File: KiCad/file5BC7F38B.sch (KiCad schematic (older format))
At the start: 74 parts, among them J301 DB9_Female, J302 Conn_01x06, J303 DB9_Male, P301 ISP/PDI, P302 Thru, P304 Header, Q301 PN2222A, SW301 SPST, U301 DS3231, U302 ATmega1284P-AU, U303 LP2992, U304 SI5351A, U305 74HC1G08, U306 LP2992, U307 SN74CB3Q3305, U308 LP2992, X301 ASTX-H11-25.MHZ, Y301 20 MHz

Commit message: AVR128DA48 Redesign
Kicad updates for new FlexFox design
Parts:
- removed TP301: I2C1, Pin_Headers:Pin_Header_Straight_1x03, symbol Connector_Generic:Conn_01x03
- removed U302: ATmega1284P-AU, Housings_QFP:TQFP-44_10x10mm_Pitch0.8mm, symbol MCU_Microchip_ATmega:ATmega1284P-AU
- removed U306: LP2992, TO_SOT_Packages_SMD:SOT-23-5, symbol Regulator_Linear:LP2992
- removed U307: SN74CB3Q3305, Housings_SSOP:TSSOP-8_3x3mm_Pitch0.65mm, symbol Interface:SN74CB3Q3305
- removed W301: TEST_1P, Measurement_Points:Measurement_Point_Square-SMD-Pad_Small, symbol FlexFox80-rescue:TEST_1P-ARDF-2-Band-MiniTx-rescue
- removed Y301: 20 MHz, Crystals:CSTNE20M0V53Z000R0, symbol Device:Resonator_Small
- added J304: Conn_01x10, symbol Connector_Generic:Conn_01x10
- added R314: 560k, Resistors_SMD:R_0805, symbol Device:R
- added R315, R316: 10k, Resistors_SMD:R_0805, symbol Device:R
- added TP301: I2C1, Pin_Headers:Pin_Header_Straight_1x04, symbol Connector_Generic:Conn_01x04
- added U302: AVR128DA48, TQFP48_PT_MCH, symbol FlexFox80-rescue:AVR128DA48-I_PT-MCU_Microchip_AVR
- added U306: LT1763CS8-5, Housings_SOIC:SOIC-8_3.9x4.9mm_Pitch1.27mm, symbol Regulator_Linear:LT1763CS8-5
- C301: LCSC Part Number (none) -> C344171
- C302, C306, C307, C308, C309, C311, C316, C319, C320: LCSC Part Number (none) -> C360619
- C303, C313, C314, C315, C317, C318: LCSC Part Number (none) -> C162420
- C304, C305: LCSC Part Number (none) -> C84416
- C310, C312: LCSC Part Number (none) -> C342818
- D301: LCSC Part Number (none) -> C152486
- D304: LCSC Part Number (none) -> C98224
- D305: LCSC Part Number (none) -> C72037
- D306, D307: LCSC Part Number (none) -> C2655331
- Q301: LCSC Part Number (none) -> C194252
- R301, R302: LCSC Part Number (none) -> C114564
- R303, R305, R306, R307, R310, R311: LCSC Part Number (none) -> C38522
- R304: LCSC Part Number (none) -> C96347
- R308, R313: LCSC Part Number (none) -> C103905
- R309: LCSC Part Number (none) -> C114561
- R312: LCSC Part Number (none) -> C352198
- RV301: LCSC Part Number (none) -> C719176
- SW301: LCSC Part Number (none) -> C221877
- U301: LCSC Part Number (none) -> C2651514
- U303, U308: value LP2992 -> LD2985BM33R; Description IC REG LINEAR 3.3V 250MA SOT23-5 -> IC REG LINEAR 3.3V 150MA SOT23-5; Digi-Key Part No. LP2992AIM5-3.3/NOPBCT-ND -> 497-3499-1-ND; LCSC Part Number (none) -> C222396; Link <a href=\"https://www.digikey.com/products/en?keywords=LP29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 -> <a href=\"https://www.digikey.com/products/en?keywords=497-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; Manufacturer Texas Instruments -> STMicroelectronics; Manufacturer PN LP2992AIM5-3.3/NOPB -> LD2985BM33R
- U304: LCSC Part Number (none) -> C529366
- U305: LCSC Part Number (none) -> C108694
- X301: value ASTX-H11-25.MHZ -> 25.MHZ TCXO; Description XTAL OSC TCXO 25.0000MHZ HCMOS -> XTAL OSC TCXO 25MHZ CLPSNW; Digi-Key Part No. 535-12039-1-ND -> 2780-I537-2O7-25.000MHZCT-ND; Link <a href=\"https://www.digikey.com/products/en?keywords=535-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 -> <a href=\"https://www.digikey.com/products/en?keywords=2780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; Manufacturer PN ASTX-H11-25.000MHZ-T -> I537-2O7-25.000 MHZ
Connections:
- net labels added: 32KHZ_SQUAREWAVE, ADC0, ADC1, ADC2, DAC0, DAC_OUTPUT, FET_DRIVER_ENABLE, PA3, PA4, PA5, PA6, PA7, PB5, PE2, PE3, PF2, PF3, PF4, PF5, PF6, RXD4, SCL0, SCL1, SDA0, SDA1, TXD4, WIFI_RX, WIFI_TX
- net labels removed: ADC6, DI_SCL, DI_SDA, DI_TXD0, HF_ENABLE, INT2, MISO, MOSI, PB3, PC2, PC3, PD4, PD5, PD6, PD7, RXD0, SCK, SCL, SDA, TXD0
- wire segments 314 -> 334
- no-connect marks 22 -> 24
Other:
- note added: "FTDI SERIAL ADAPTER"
- note added: "Future Display Interface"
- note removed: "FTDI PROGRAMMING ADAPTER"
- moved on the sheet: D304, D305, J302, J303, P301, R301, R302, R304, SW301, TP302

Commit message: Updates for AVR128DA48
o Board changes
o Gerbers updated
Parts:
- removed C304: 10uF, Capacitors_SMD:C_0805, symbol Device:C_Small
- removed C309, C316: 100nF, Capacitors_SMD:C_0805, symbol Device:C_Small
- removed unit 2 of D301
- removed R305: 10k, Resistors_SMD:R_0805, symbol Device:R
- added J305, J306, J307: Conn_01x02, Pin_Headers:Pin_Header_Straight_1x02, symbol Connector_Generic:Conn_01x02
- J304: footprint (none) -> Pin_Headers:Pin_Header_Straight_1x10; Digi-Key Part No. (none) -> np; Link (none) -> np; Manufacturer (none) -> np
- U302: footprint TQFP48_PT_MCH -> Housings_QFP:TQFP-48_7x7mm_Pitch0.5mm
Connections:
- net GND: now also J305.1 (Pin_1), J306.1 (Pin_1), J307.1 (Pin_1)
- net PC7: now also J305.2 (Pin_2)
- net at D305.2 (A), R302.1: now also J306.2 (Pin_2)
- net at D304.2 (A), R301.1: now also J307.2 (Pin_2)
- net ~RESET~ renamed PF6
- no-connect marks 24 -> 26
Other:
- moved on the sheet: D304, D305, R301, R302, SW301, TP302

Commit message: Updates
o Added fan control
o Fixed pinout for load switch device
o Updated gerbers
o Updated BOM
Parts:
- added C304: 10uF, Capacitors_SMD:C_0805, symbol Device:C_Small
- added J308: Conn_01x02, Pin_Headers:Pin_Header_Straight_1x02, symbol Connector_Generic:Conn_01x02
- added U307: TPS22810DBVT, TO_SOT_Packages_SMD:SOT-23-6, symbol Power_Management:TPS22810DBVT
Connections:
- net GND: now also C304.2, U307.2 (GND)
- net PA1 renamed FAN_ENABLE
- net FAN_ENABLE: now also U307.3 (EN/UVLO)
- new net: J308.2 (Pin_2), U307.1 (VIN)
- new net: C304.1, J308.1 (Pin_1), U307.6 (VOUT)
- no-connect marks 26 -> 27
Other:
- note added: "OPTIONAL FAN CONTROL"
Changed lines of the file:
@@
 Connection ~ 8150 7050
 NoConn ~ 7800 4150
-NoConn ~ 7800 4050
 Text Notes 1400 4800 1    39   ~ 8
 I2C pull-ups can be provided by uC \nport pin pull-ups on SCL and SDA.
@@
 Wire Wire Line
 	10950 5600 10950 5300
-Wire Bus Line
-	7700 3300 7700 8000
 Connection ~ 10950 5300
 Wire Wire Line
@@
 	0    1    1    0
 $EndComp
+$Comp
+L Power_Management:TPS22810DBVT U307
+U 1 1 6203E823
+P 15100 3900
+F 0 "U307" H 15100 4267 50  0000 C CNN
+F 1 "TPS22810DBVT" H 15100 4176 50  0000 C CNN
+F 2 "TO_SOT_Packages_SMD:SOT-23-6" H 15100 3200 50  0001 C CNN
+F 3 "http://www.ti.com/lit/ds/symlink/tps22810.pdf" H 15100 3900 50  0001 C CNN
+F 4 "296-45304-1-ND" H 15100 3900 50  0001 C CNN "Digi-Key Part No."
+F 5 "<a href=\"https://www.digikey.com/products/en?keywords=296-45304-1-ND\">Link</a>" H 15100 3900 50  0001 C CNN "Link"
+F 6 "Texas Instruments" H 15100 3900 50  0001 C CNN "Manufacturer"
+F 7 "TPS22810DBVT" H 15100 3900 50  0001 C CNN "Manufacturer PN"
+F 8 "IC PWR SWITCH N-CHAN 1:1 SOT23-6" H 15100 3900 50  0001 C CNN "Description"
+F 9 "C2680364" H 15100 3900 50  0001 C CNN "LCSC Part Number"
+	1    15100 3900
+	1    0    0    -1
+$EndComp
+Text GLabel 7950 4050 2    39   Output ~ 0
+FAN_ENABLE
+Wire Wire Line
+	7800 4050 7950 4050
+Text GLabel 14700 3900 0    39   Input ~ 0
+FAN_ENABLE
+$Comp
+L power:GNDD #PWR0309
+U 1 1 62087421
+P 15100 4200
+F 0 "#PWR0309" H 15100 3950 50  0001 C CNN
+F 1 "GNDD" H 15100 4050 50  0000 C CNN
+F 2 "" H 15100 4200 50  0000 C CNN
+F 3 "" H 15100 4200 50  0000 C CNN
+	1    15100 4200
+	1    0    0    -1
+$EndComp
+$Comp
+L Connector_Generic:Conn_01x02 J308
+U 1 1 6208B0C7
+P 15700 3700
+F 0 "J308" H 15850 3650 50  0000 C CNN
+F 1 "Conn_01x02" H 15618 3466 50  0001 C CNN
+F 2 "Pin_Headers:Pin_Header_Straight_1x02" H 15700 3700 50  0001 C CNN
+F 3 "" H 15700 3700 50  0001 C CNN
+F 4 "np" H 15700 3700 50  0001 C CNN "Digi-Key Part No."
+F 5 "np" H 15700 3700 50  0001 C CNN "Link"
+F 6 "np" H 15700 3700 50  0001 C CNN "Manufacturer"
+	1    15700 3700
+	1    0    0    -1
+$EndComp
+Wire Wire Line
+	14700 3800 14500 3800
+Wire Wire Line
+	14500 3800 14500 3600
+Wire Wire Line
+	14500 3400 15500 3400
+Wire Wire Line
+	15500 3400 15500 3700
+NoConn ~ 15500 3900
+NoConn ~ 15500 4000
+$Comp
+L Device:C_Small C304
+U 1 1 620FA271
+P 14300 3600
+F 0 "C304" V 14071 3600 50  0000 C CNN
+F 1 "10uF" V 14162 3600 50  0000 C CNN
+F 2 "Capacitors_SMD:C_0805" H 14300 3600 50  0001 C CNN
+F 3 "" H 14300 3600 50  0001 C CNN
+F 4 "490-5523-1-ND" H 14300 3600 50  0001 C CNN "Digi-Key Part No."
+F 5 "<a href=\"https://www.digikey.com/products/en?keywords=490-5523-1-ND\">Link</a>" H 14300 3600 50  0001 C CNN "Link"
+F 6 "Murata Electronics" H 14300 3600 50  0001 C CNN "Manufacturer"
+F 7 "GRM21BR61E106KA73L" H 14300 3600 50  0001 C CNN "Manufacturer PN"
+F 8 "CAP CER 10UF 25V X5R 0805" H 14300 3600 50  0001 C CNN "Description"
+F 9 "C84416" H 14300 3600 50  0001 C CNN "LCSC Part Number"
+	1    14300 3600
+	0    1    1    0
+$EndComp
+$Comp
+L power:GNDD #PWR0308
+U 1 1 620FFD9F
+P 14200 3600
+F 0 "#PWR0308" H 14200 3350 50  0001 C CNN
+F 1 "GNDD" H 14200 3450 50  0000 C CNN
+F 2 "" H 14200 3600 50  0000 C CNN
+F 3 "" H 14200 3600 50  0000 C CNN
+	1    14200 3600
+	0    1    1    0
+$EndComp
+Wire Wire Line
+	14400 3600 14500 3600
+Connection ~ 14500 3600
+Wire Wire Line
+	14500 3600 14500 3400
+Wire Notes Line
+	13800 3000 13800 4550
+Wire Notes Line
+	13800 4550 16000 4550
+Wire Notes Line
+	16000 4550 16000 3000
+Wire Notes Line
+	16000 3000 13800 3000
+Text Notes 14300 2950 0    61   ~ 12
+OPTIONAL FAN CONTROL
+Wire Bus Line
+	7700 3300 7700 8000
 $EndSCHEMATC

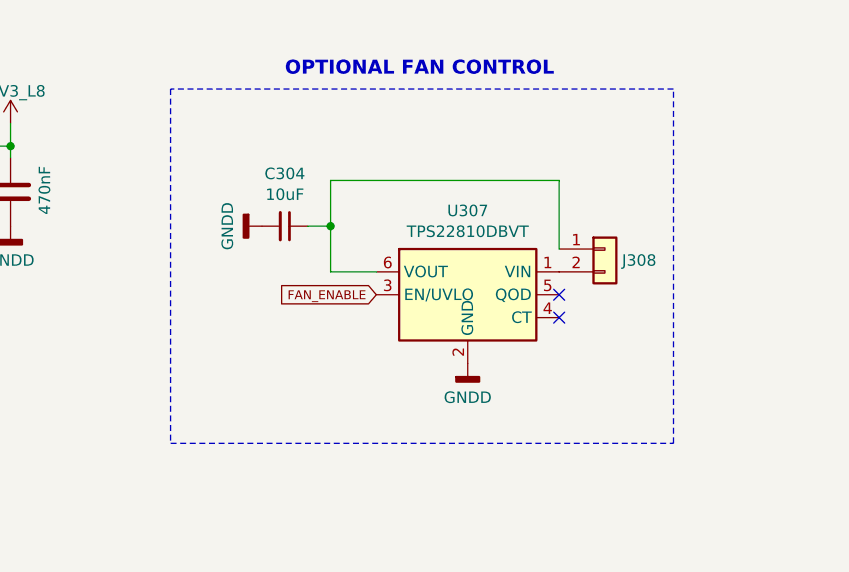
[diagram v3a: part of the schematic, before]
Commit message: Fan Control Update
o Corrected an error in the fan control circuit
o Updated all gerbers and fab files
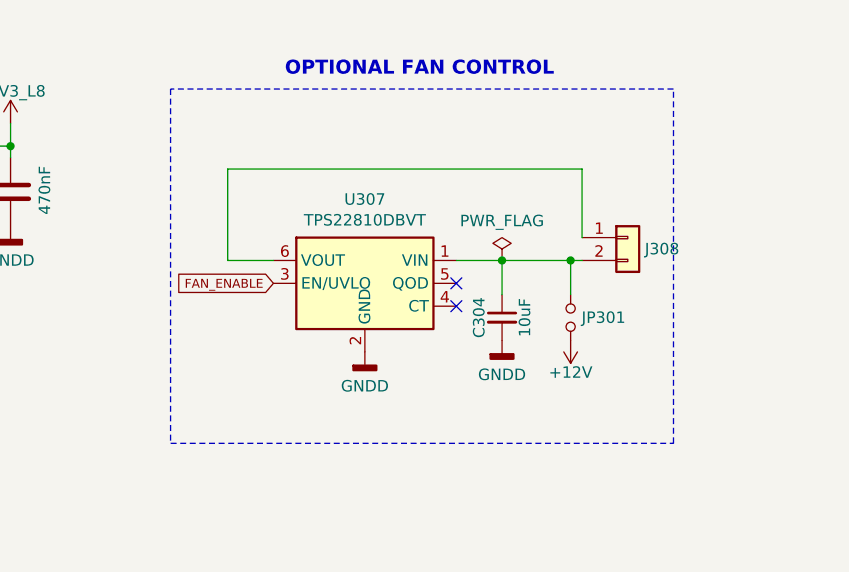
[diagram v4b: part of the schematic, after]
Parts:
- added JP301: Jumper_NO_Small, Wire_Connections_Bridges:Solder-Jumper-NO-SMD-Pad_Small, symbol Device:Jumper_NO_Small
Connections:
- net +12V: now also JP301.2
- net at J308.2 (Pin_2), U307.1 (VIN): now also C304.1, JP301.1
- net at J308.1 (Pin_1), U307.6 (VOUT): no longer C304.1
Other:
- moved on the sheet: C304, J308, U307
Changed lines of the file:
@@
 L Power_Management:TPS22810DBVT U307
 U 1 1 6203E823
-P 15100 3900
-F 0 "U307" H 15100 4267 50  0000 C CNN
-F 1 "TPS22810DBVT" H 15100 4176 50  0000 C CNN
-F 2 "TO_SOT_Packages_SMD:SOT-23-6" H 15100 3200 50  0001 C CNN
-F 3 "http://www.ti.com/lit/ds/symlink/tps22810.pdf" H 15100 3900 50  0001 C CNN
-F 4 "296-45304-1-ND" H 15100 3900 50  0001 C CNN "Digi-Key Part No."
-F 5 "<a href=\"https://www.digikey.com/products/en?keywords=296-45304-1-ND\">Link</a>" H 15100 3900 50  0001 C CNN "Link"
-F 6 "Texas Instruments" H 15100 3900 50  0001 C CNN "Manufacturer"
-F 7 "TPS22810DBVT" H 15100 3900 50  0001 C CNN "Manufacturer PN"
-F 8 "IC PWR SWITCH N-CHAN 1:1 SOT23-6" H 15100 3900 50  0001 C CNN "Description"
-F 9 "C2680364" H 15100 3900 50  0001 C CNN "LCSC Part Number"
-	1    15100 3900
+P 14650 3850
+F 0 "U307" H 14650 4217 50  0000 C CNN
+F 1 "TPS22810DBVT" H 14650 4126 50  0000 C CNN
+F 2 "TO_SOT_Packages_SMD:SOT-23-6" H 14650 3150 50  0001 C CNN
+F 3 "http://www.ti.com/lit/ds/symlink/tps22810.pdf" H 14650 3850 50  0001 C CNN
+F 4 "296-45304-1-ND" H 14650 3850 50  0001 C CNN "Digi-Key Part No."
+F 5 "<a href=\"https://www.digikey.com/products/en?keywords=296-45304-1-ND\">Link</a>" H 14650 3850 50  0001 C CNN "Link"
+F 6 "Texas Instruments" H 14650 3850 50  0001 C CNN "Manufacturer"
+F 7 "TPS22810DBVT" H 14650 3850 50  0001 C CNN "Manufacturer PN"
+F 8 "IC PWR SWITCH N-CHAN 1:1 SOT23-6" H 14650 3850 50  0001 C CNN "Description"
+F 9 "C2680364" H 14650 3850 50  0001 C CNN "LCSC Part Number"
+	1    14650 3850
 	1    0    0    -1
 $EndComp
@@
 Wire Wire Line
 	7800 4050 7950 4050
-Text GLabel 14700 3900 0    39   Input ~ 0
+Text GLabel 14250 3850 0    39   Input ~ 0
 FAN_ENABLE
 $Comp
 L power:GNDD #PWR0309
 U 1 1 62087421
-P 15100 4200
-F 0 "#PWR0309" H 15100 3950 50  0001 C CNN
-F 1 "GNDD" H 15100 4050 50  0000 C CNN
-F 2 "" H 15100 4200 50  0000 C CNN
-F 3 "" H 15100 4200 50  0000 C CNN
-	1    15100 4200
+P 14650 4150
+F 0 "#PWR0309" H 14650 3900 50  0001 C CNN
+F 1 "GNDD" H 14650 4000 50  0000 C CNN
+F 2 "" H 14650 4150 50  0000 C CNN
+F 3 "" H 14650 4150 50  0000 C CNN
+	1    14650 4150
 	1    0    0    -1
 $EndComp
@@
 L Connector_Generic:Conn_01x02 J308
 U 1 1 6208B0C7
-P 15700 3700
-F 0 "J308" H 15850 3650 50  0000 C CNN
-F 1 "Conn_01x02" H 15618 3466 50  0001 C CNN
-F 2 "Pin_Headers:Pin_Header_Straight_1x02" H 15700 3700 50  0001 C CNN
-F 3 "" H 15700 3700 50  0001 C CNN
-F 4 "np" H 15700 3700 50  0001 C CNN "Digi-Key Part No."
-F 5 "np" H 15700 3700 50  0001 C CNN "Link"
-F 6 "np" H 15700 3700 50  0001 C CNN "Manufacturer"
-	1    15700 3700
+P 15800 3650
+F 0 "J308" H 15950 3600 50  0000 C CNN
+F 1 "Conn_01x02" H 15718 3416 50  0001 C CNN
+F 2 "Pin_Headers:Pin_Header_Straight_1x02" H 15800 3650 50  0001 C CNN
+F 3 "" H 15800 3650 50  0001 C CNN
+F 4 "np" H 15800 3650 50  0001 C CNN "Digi-Key Part No."
+F 5 "np" H 15800 3650 50  0001 C CNN "Link"
+F 6 "np" H 15800 3650 50  0001 C CNN "Manufacturer"
+	1    15800 3650
 	1    0    0    -1
 $EndComp
 Wire Wire Line
-	14700 3800 14500 3800
+	14250 3750 14050 3750
 Wire Wire Line
-	14500 3800 14500 3600
+	14050 3350 15600 3350
 Wire Wire Line
-	14500 3400 15500 3400
-Wire Wire Line
-	15500 3400 15500 3700
-NoConn ~ 15500 3900
-NoConn ~ 15500 4000
+	15600 3350 15600 3650
+NoConn ~ 15050 3850
+NoConn ~ 15050 3950
 $Comp
 L Device:C_Small C304
 U 1 1 620FA271
-P 14300 3600
-F 0 "C304" V 14071 3600 50  0000 C CNN
-F 1 "10uF" V 14162 3600 50  0000 C CNN
-F 2 "Capacitors_SMD:C_0805" H 14300 3600 50  0001 C CNN
-F 3 "" H 14300 3600 50  0001 C CNN
-F 4 "490-5523-1-ND" H 14300 3600 50  0001 C CNN "Digi-Key Part No."
-F 5 "<a href=\"https://www.digikey.com/products/en?keywords=490-5523-1-ND\">Link</a>" H 14300 3600 50  0001 C CNN "Link"
-F 6 "Murata Electronics" H 14300 3600 50  0001 C CNN "Manufacturer"
-F 7 "GRM21BR61E106KA73L" H 14300 3600 50  0001 C CNN "Manufacturer PN"
-F 8 "CAP CER 10UF 25V X5R 0805" H 14300 3600 50  0001 C CNN "Description"
-F 9 "C84416" H 14300 3600 50  0001 C CNN "LCSC Part Number"
-	1    14300 3600
-	0    1    1    0
+P 15250 4000
+F 0 "C304" V 15150 4000 50  0000 C CNN
+F 1 "10uF" V 15350 4000 50  0000 C CNN
+F 2 "Capacitors_SMD:C_0805" H 15250 4000 50  0001 C CNN
+F 3 "" H 15250 4000 50  0001 C CNN
+F 4 "490-5523-1-ND" H 15250 4000 50  0001 C CNN "Digi-Key Part No."
+F 5 "<a href=\"https://www.digikey.com/products/en?keywords=490-5523-1-ND\">Link</a>" H 15250 4000 50  0001 C CNN "Link"
+F 6 "Murata Electronics" H 15250 4000 50  0001 C CNN "Manufacturer"
+F 7 "GRM21BR61E106KA73L" H 15250 4000 50  0001 C CNN "Manufacturer PN"
+F 8 "CAP CER 10UF 25V X5R 0805" H 15250 4000 50  0001 C CNN "Description"
+F 9 "C84416" H 15250 4000 50  0001 C CNN "LCSC Part Number"
+	1    15250 4000
+	1    0    0    -1
 $EndComp
 $Comp
 L power:GNDD #PWR0308
 U 1 1 620FFD9F
-P 14200 3600
-F 0 "#PWR0308" H 14200 3350 50  0001 C CNN
-F 1 "GNDD" H 14200 3450 50  0000 C CNN
-F 2 "" H 14200 3600 50  0000 C CNN
-F 3 "" H 14200 3600 50  0000 C CNN
-	1    14200 3600
-	0    1    1    0
+P 15250 4100
+F 0 "#PWR0308" H 15250 3850 50  0001 C CNN
+F 1 "GNDD" H 15250 3950 50  0000 C CNN
+F 2 "" H 15250 4100 50  0000 C CNN
+F 3 "" H 15250 4100 50  0000 C CNN
+	1    15250 4100
+	1    0    0    -1
 $EndComp
-Wire Wire Line
-	14400 3600 14500 3600
-Connection ~ 14500 3600
-Wire Wire Line
-	14500 3600 14500 3400
 Wire Notes Line
 	13800 3000 13800 4550
@@
 Text Notes 14300 2950 0    61   ~ 12
 OPTIONAL FAN CONTROL
+$Comp
+L Device:Jumper_NO_Small JP301
+U 1 1 6206C578
+P 15550 4000
+F 0 "JP301" V 15550 4048 50  0000 L CNN
+F 1 "Jumper_NO_Small" V 15595 4048 50  0001 L CNN
+F 2 "Wire_Connections_Bridges:Solder-Jumper-NO-SMD-Pad_Small" H 15550 4000 50  0001 C CNN
+F 3 "" H 15550 4000 50  0001 C CNN
+F 4 "np" H 15550 4000 50  0001 C CNN "Digi-Key Part No."
+F 5 "np" H 15550 4000 50  0001 C CNN "Link"
+F 6 "np" H 15550 4000 50  0001 C CNN "Manufacturer"
+	1    15550 4000
+	0    1    1    0
+$EndComp
+$Comp
+L power:+12V #PWR0138
+U 1 1 6206E6FC
+P 15550 4100
+F 0 "#PWR0138" H 15550 3950 50  0001 C CNN
+F 1 "+12V" H 15550 4240 50  0000 C CNN
+F 2 "" H 15550 4100 50  0000 C CNN
+F 3 "" H 15550 4100 50  0000 C CNN
+	1    15550 4100
+	1    0    0    1
+$EndComp
+Wire Wire Line
+	15550 3900 15550 3750
+Wire Wire Line
+	14050 3350 14050 3750
+Wire Wire Line
+	15250 3900 15250 3750
+Wire Wire Line
+	15050 3750 15250 3750
+Connection ~ 15250 3750
+Wire Wire Line
+	15250 3750 15550 3750
+Connection ~ 15550 3750
+Wire Wire Line
+	15550 3750 15600 3750
+$Comp
+L power:PWR_FLAG #FLG0108
+U 1 1 6222EECD
+P 15250 3750
+F 0 "#FLG0108" H 15250 3825 50  0001 C CNN
+F 1 "PWR_FLAG" H 15250 3923 50  0000 C CNN
+F 2 "" H 15250 3750 50  0001 C CNN
+F 3 "~" H 15250 3750 50  0001 C CNN
+	1    15250 3750
+	1    0    0    -1
+$EndComp
 Wire Bus Line
 	7700 3300 7700 8000

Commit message: Schematic Update
Updated footprint specified for AVR128DA48
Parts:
- U302: footprint Housings_QFP:TQFP-48_7x7mm_Pitch0.5mm -> Housings_QFP:TQFP-48_7x7mm_Pitch0.5mm_AVR128DA48
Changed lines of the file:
@@
 F 0 "U302" H 6500 1900 60  0000 C CNB
 F 1 "AVR128DA48" H 6500 1700 60  0000 C CNB
-F 2 "Housings_QFP:TQFP-48_7x7mm_Pitch0.5mm" H 6350 3740 60  0001 C CNN
+F 2 "Housings_QFP:TQFP-48_7x7mm_Pitch0.5mm_AVR128DA48" H 6350 3740 60  0001 C CNN
 F 3 "" H 5150 3500 60  0000 C CNN
 F 4 "150-AVR128DA48T-E/PTCT-ND" H 5150 3500 50  0001 C CNN "Digi-Key Part No."

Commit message: Updates
o BOM updates
o Gerber updates
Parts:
- U306: Description (none) -> IC REG LINEAR 5V 500MA 8SOIC; Digi-Key Part No. (none) -> LT1763CS8-5#TRPBFCT-ND; LCSC Part Number (none) -> C193629; Link (none) -> <a href=\"https://www.digikey.com/products/en?keywords=LT17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; Manufacturer (none) -> Analog Devices Inc.; Manufacturer PN (none) -> LT1763CS8-5#TRPBF
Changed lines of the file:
@@
 F 2 "Housings_SOIC:SOIC-8_3.9x4.9mm_Pitch1.27mm" H 14775 6600 50  0001 L CIN
 F 3 "" H 14750 6850 50  0001 C CNN
+F 4 "LT1763CS8-5#TRPBFCT-ND" H 14750 6850 50  0001 C CNN "Digi-Key Part No."
+F 5 "<a href=\"https://www.digikey.com/products/en?keywords=LT1763CS8-5#TRPBFCT-ND\">Link</a>" H 14750 6850 50  0001 C CNN "Link"
+F 6 "Analog Devices Inc." H 14750 6850 50  0001 C CNN "Manufacturer"
+F 7 "LT1763CS8-5#TRPBF" H 14750 6850 50  0001 C CNN "Manufacturer PN"
+F 8 "IC REG LINEAR 5V 500MA 8SOIC" H 14750 6850 50  0001 C CNN "Description"
+F 9 "C193629" H 14750 6850 50  0001 C CNN "LCSC Part Number"
 	1    14750 6850
 	-1   0    0    -1

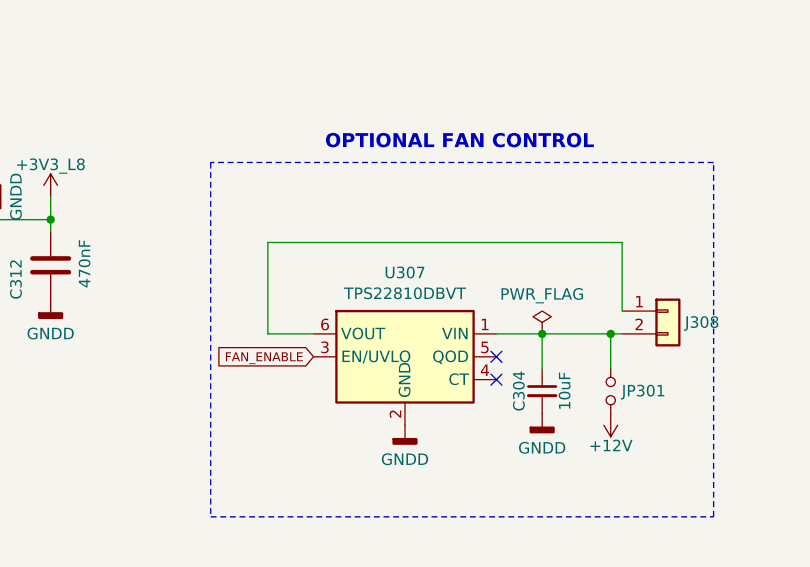
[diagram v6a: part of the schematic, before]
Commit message: Footprint Updates
Tweaks to PCB footprints.
Removed solder paste from unpopulated components
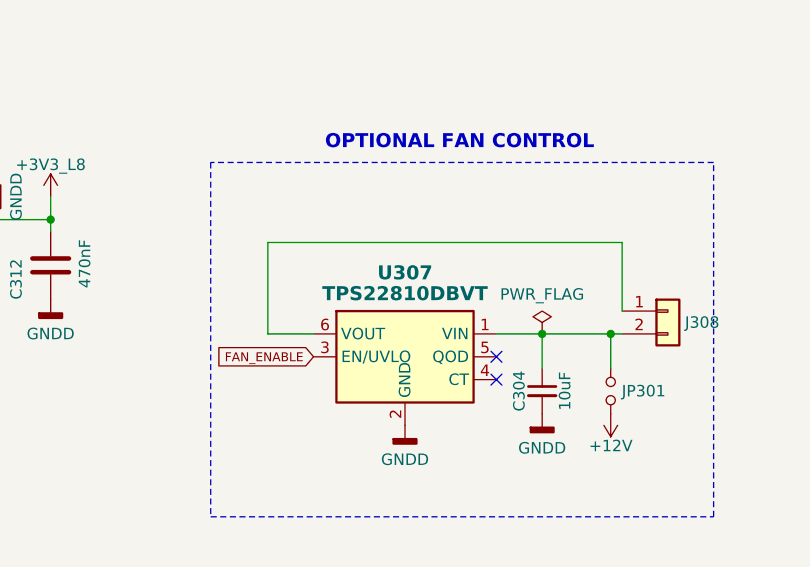
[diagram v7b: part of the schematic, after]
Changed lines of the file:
@@
 U 1 1 6203E823
 P 14650 3850
-F 0 "U307" H 14650 4217 50  0000 C CNN
-F 1 "TPS22810DBVT" H 14650 4126 50  0000 C CNN
+F 0 "U307" H 14650 4217 61  0000 C CNB
+F 1 "TPS22810DBVT" H 14650 4126 61  0000 C CNB
 F 2 "TO_SOT_Packages_SMD:SOT-23-6" H 14650 3150 50  0001 C CNN
 F 3 "http://www.ti.com/lit/ds/symlink/tps22810.pdf" H 14650 3850 50  0001 C CNN
